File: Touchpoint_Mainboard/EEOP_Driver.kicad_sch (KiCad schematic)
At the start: 3 parts, among them J701 Conn_01x32, J702 Conn_01x32, U701 HV507PG-G

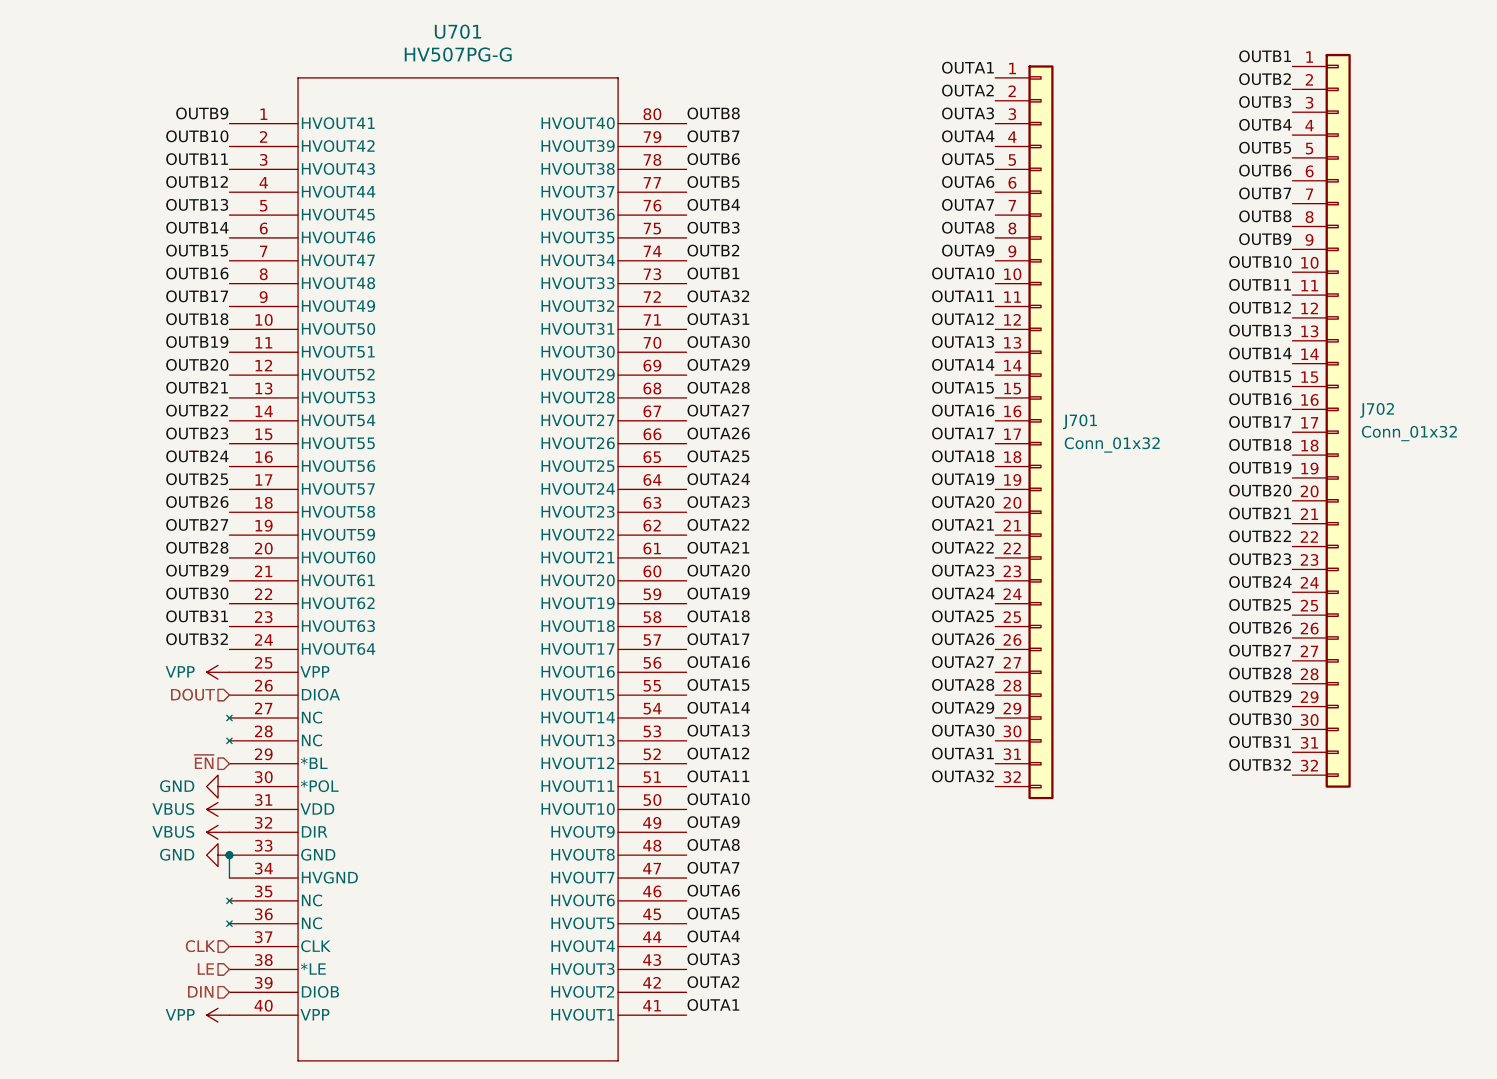
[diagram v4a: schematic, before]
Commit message: Finally finished routing EEOP driver
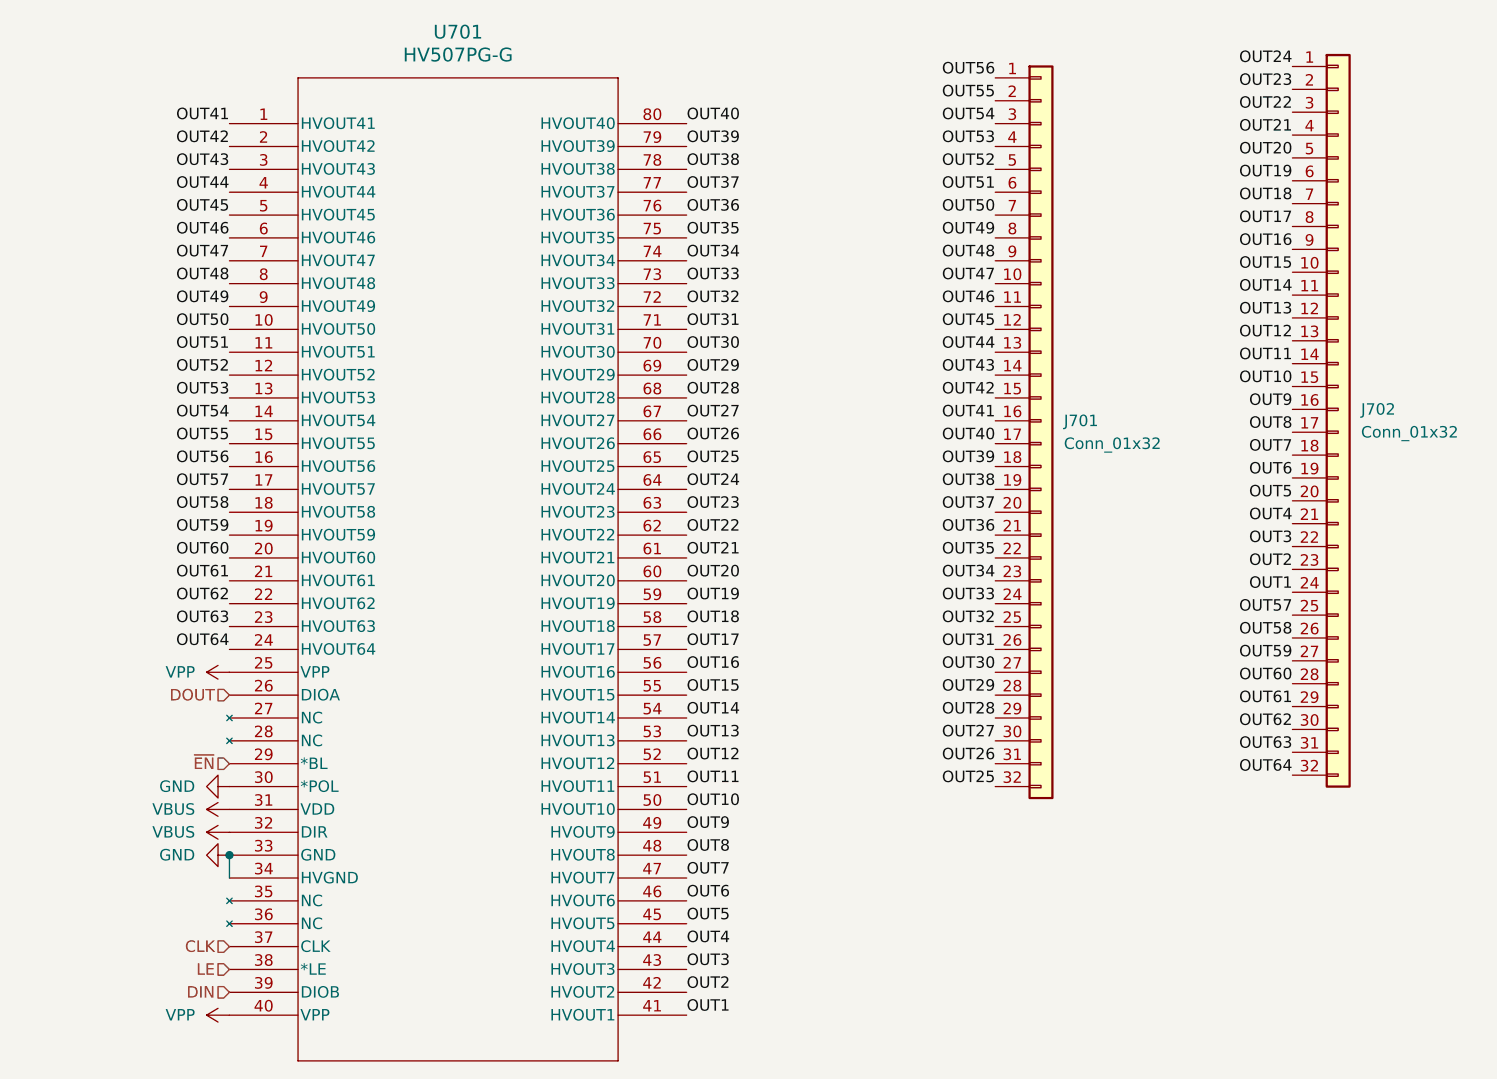
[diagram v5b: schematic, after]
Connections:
- net OUTA1 renamed OUT1
- net OUT1: now also J702.24 (Pin_24); no longer J701.1 (Pin_1)
- net OUTA10 renamed OUT10
- net OUT10: now also J702.15 (Pin_15); no longer J701.10 (Pin_10)
- net OUTA11 renamed OUT11
- net OUT11: now also J702.14 (Pin_14); no longer J701.11 (Pin_11)
- net OUTA12 renamed OUT12
- net OUT12: now also J702.13 (Pin_13); no longer J701.12 (Pin_12)
- net OUTA13 renamed OUT13
- net OUT13: now also J702.12 (Pin_12); no longer J701.13 (Pin_13)
- net OUTA14 renamed OUT14
- net OUT14: now also J702.11 (Pin_11); no longer J701.14 (Pin_14)
- net OUTA15 renamed OUT15
- net OUT15: now also J702.10 (Pin_10); no longer J701.15 (Pin_15)
- net OUTA16 renamed OUT16
- net OUT16: now also J702.9 (Pin_9); no longer J701.16 (Pin_16)
- net OUTA17 renamed OUT17
- net OUT17: now also J702.8 (Pin_8); no longer J701.17 (Pin_17)
- net OUTA18 renamed OUT18
- net OUT18: now also J702.7 (Pin_7); no longer J701.18 (Pin_18)
- net OUTA19 renamed OUT19
- net OUT19: now also J702.6 (Pin_6); no longer J701.19 (Pin_19)
- net OUTA2 renamed OUT2
- net OUT2: now also J702.23 (Pin_23); no longer J701.2 (Pin_2)
- net OUTA20 renamed OUT20
- net OUT20: now also J702.5 (Pin_5); no longer J701.20 (Pin_20)
- net OUTA21 renamed OUT21
- net OUT21: now also J702.4 (Pin_4); no longer J701.21 (Pin_21)
- net OUTA22 renamed OUT22
- net OUT22: now also J702.3 (Pin_3); no longer J701.22 (Pin_22)
- net OUTA23 renamed OUT23
- net OUT23: now also J702.2 (Pin_2); no longer J701.23 (Pin_23)
- net OUTA24 renamed OUT24
- net OUT24: now also J702.1 (Pin_1); no longer J701.24 (Pin_24)
- net OUTA25 renamed OUT25
- net OUT25: now also J701.32 (Pin_32); no longer J701.25 (Pin_25)
- net OUTA26 renamed OUT26
- net OUT26: now also J701.31 (Pin_31); no longer J701.26 (Pin_26)
- net OUTA27 renamed OUT27
- net OUT27: now also J701.30 (Pin_30); no longer J701.27 (Pin_27)
- net OUTA28 renamed OUT28
- net OUT28: now also J701.29 (Pin_29); no longer J701.28 (Pin_28)
- net OUTA29 renamed OUT29
- net OUT29: now also J701.28 (Pin_28); no longer J701.29 (Pin_29)
- net OUTA3 renamed OUT3
- net OUT3: now also J702.22 (Pin_22); no longer J701.3 (Pin_3)
- net OUTA30 renamed OUT30
- net OUT30: now also J701.27 (Pin_27); no longer J701.30 (Pin_30)
- net OUTA31 renamed OUT31
- net OUT31: now also J701.26 (Pin_26); no longer J701.31 (Pin_31)
- net OUTA32 renamed OUT32
- net OUT32: now also J701.25 (Pin_25); no longer J701.32 (Pin_32)
- net OUTA4 renamed OUT4
- net OUT4: now also J702.21 (Pin_21); no longer J701.4 (Pin_4)
- net OUTA5 renamed OUT5
- net OUT5: now also J702.20 (Pin_20); no longer J701.5 (Pin_5)
- net OUTA6 renamed OUT51
- net OUT51: now also U701.11 (HVOUT51); no longer U701.46 (HVOUT6)
- net OUTA7 renamed OUT50
- net OUT50: now also U701.10 (HVOUT50); no longer U701.47 (HVOUT7)
- net OUTA8 renamed OUT49
- net OUT49: now also U701.9 (HVOUT49); no longer U701.48 (HVOUT8)
- net OUTA9 renamed OUT48
- net OUT48: now also U701.8 (HVOUT48); no longer U701.49 (HVOUT9)
- net OUTB1 renamed OUT33
- net OUT33: now also J701.24 (Pin_24); no longer J702.1 (Pin_1)
- net OUTB10 renamed OUT42
- net OUT42: now also J701.15 (Pin_15); no longer J702.10 (Pin_10)
- net OUTB11 renamed OUT43
- net OUT43: now also J701.14 (Pin_14); no longer J702.11 (Pin_11)
- net OUTB12 renamed OUT44
- net OUT44: now also J701.13 (Pin_13); no longer J702.12 (Pin_12)
- net OUTB13 renamed OUT45
- net OUT45: now also J701.12 (Pin_12); no longer J702.13 (Pin_13)
- net OUTB14 renamed OUT46
- net OUT46: now also J701.11 (Pin_11); no longer J702.14 (Pin_14)
- net OUTB15 renamed OUT47
- net OUT47: now also J701.10 (Pin_10); no longer J702.15 (Pin_15)
- net OUTB16 renamed OUT9
- net OUT9: now also U701.49 (HVOUT9); no longer U701.8 (HVOUT48)
- net OUTB17 renamed OUT8
- net OUT8: now also U701.48 (HVOUT8); no longer U701.9 (HVOUT49)
- net OUTB18 renamed OUT7
- net OUT7: now also U701.47 (HVOUT7); no longer U701.10 (HVOUT50)
- net OUTB19 renamed OUT6
- net OUT6: now also U701.46 (HVOUT6); no longer U701.11 (HVOUT51)
- net OUTB2 renamed OUT34
- net OUT34: now also J701.23 (Pin_23); no longer J702.2 (Pin_2)
- net OUTB20 renamed OUT52
- net OUT52: now also J701.5 (Pin_5); no longer J702.20 (Pin_20)
- net OUTB21 renamed OUT53
- net OUT53: now also J701.4 (Pin_4); no longer J702.21 (Pin_21)
- net OUTB22 renamed OUT54
- net OUT54: now also J701.3 (Pin_3); no longer J702.22 (Pin_22)
- net OUTB23 renamed OUT55
- net OUT55: now also J701.2 (Pin_2); no longer J702.23 (Pin_23)
- net OUTB24 renamed OUT56
- net OUT56: now also J701.1 (Pin_1); no longer J702.24 (Pin_24)
- net OUTB25 renamed OUT57
- net OUTB26 renamed OUT58
- net OUTB27 renamed OUT59
- net OUTB28 renamed OUT60
- net OUTB29 renamed OUT61
- net OUTB3 renamed OUT35
- net OUT35: now also J701.22 (Pin_22); no longer J702.3 (Pin_3)
- net OUTB30 renamed OUT62
- net OUTB31 renamed OUT63
- net OUTB32 renamed OUT64
- net OUTB4 renamed OUT36
- net OUT36: now also J701.21 (Pin_21); no longer J702.4 (Pin_4)
- net OUTB5 renamed OUT37
- net OUT37: now also J701.20 (Pin_20); no longer J702.5 (Pin_5)
- net OUTB6 renamed OUT38
- net OUT38: now also J701.19 (Pin_19); no longer J702.6 (Pin_6)
- net OUTB7 renamed OUT39
- net OUT39: now also J701.18 (Pin_18); no longer J702.7 (Pin_7)
- net OUTB8 renamed OUT40
- net OUT40: now also J701.17 (Pin_17); no longer J702.8 (Pin_8)
- net OUTB9 renamed OUT41
- net OUT41: now also J701.16 (Pin_16); no longer J702.9 (Pin_9)

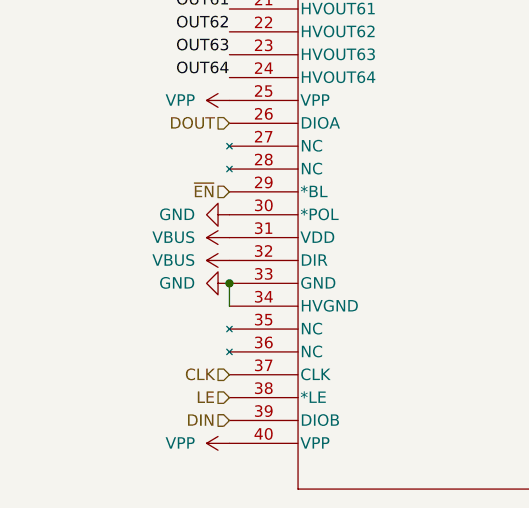
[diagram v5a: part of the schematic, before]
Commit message: Almost finished routing mainboard
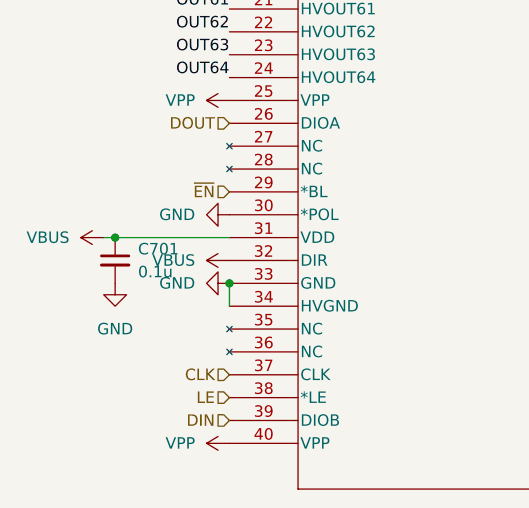
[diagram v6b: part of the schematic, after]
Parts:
- added C701: 0.1u, Capacitor_SMD:C_0402_1005Metric, symbol Device:C_Small
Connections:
- net GND: now also C701.2
- net VBUS: now also C701.1
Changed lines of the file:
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@@
 		(color 0 0 0 0)
+	)
+	(junction
+		(at 13.97 100.33)
+		(diameter 0)
+		(color 0 0 0 0)
+	)
+	(wire
+		(pts
+			(xy 13.97 100.33) (xy 26.67 100.33)
+		)
+		(stroke
+			(width 0)
+			(type default)
+		)
+	)
+	(wire
+		(pts
+			(xy 12.7 100.33) (xy 13.97 100.33)
+		)
+		(stroke
+			(width 0)
+			(type default)
+		)
 	)
 	(wire
@@
 	)
 	(symbol
+		(lib_id "Device:C_Small")
+		(at 13.97 102.87 0)
+		(unit 1)
+		(exclude_from_sim no)
+		(in_bom yes)
+		(on_board yes)
+		(dnp no)
+		(fields_autoplaced yes)
+		(property "Reference" "C701"
+			(at 16.51 101.6062 0)
+			(effects
+				(font
+					(size 1.27 1.27)
+				)
+				(justify left)
+			)
+		)
+		(property "Value" "0.1u"
+			(at 16.51 104.1462 0)
+			(effects
+				(font
+					(size 1.27 1.27)
+				)
+				(justify left)
+			)
+		)
+		(property "Footprint" "Capacitor_SMD:C_0402_1005Metric"
+			(at 13.97 102.87 0)
+			(effects
+				(font
+					(size 1.27 1.27)
+				)
+				(hide yes)
+			)
+		)
+		(property "Datasheet" "~"
+			(at 13.97 102.87 0)
+			(effects
+				(font
+					(size 1.27 1.27)
+				)
+				(hide yes)
+			)
+		)
+		(property "Description" "Unpolarized capacitor, small symbol"
+			(at 13.97 102.87 0)
+			(effects
+				(font
+					(size 1.27 1.27)
+				)
+				(hide yes)
+			)
+		)
+		(pin "2"
+		)
+		(pin "1"
+		)
+		(instances
+			(project "Touchpoint_Mainboard"
+				(path "/f37b5f88-420a-4646-85df-8f9851d23e3c/d77d4631-394e-42d9-bdcc-1bd3eb66f861"
+					(reference "C701")
+					(unit 1)
+				)
+			)
+		)
+	)
+	(symbol
+		(lib_id "power:GND")
+		(at 13.97 105.41 0)
+		(unit 1)
+		(exclude_from_sim no)
+		(in_bom yes)
+		(on_board yes)
+		(dnp no)
+		(fields_autoplaced yes)
+		(property "Reference" "#PWR0707"
+			(at 13.97 111.76 0)
+			(effects
+				(font
+					(size 1.27 1.27)
+				)
+				(hide yes)
+			)
+		)
+		(property "Value" "GND"
+			(at 13.97 110.49 0)
+			(effects
+				(font
+					(size 1.27 1.27)
+				)
+			)
+		)
+		(property "Footprint" ""
+			(at 13.97 105.41 0)
+			(effects
+				(font
+					(size 1.27 1.27)
+				)
+				(hide yes)
+			)
+		)
+		(property "Datasheet" ""
+			(at 13.97 105.41 0)
+			(effects
+				(font
+					(size 1.27 1.27)
+				)
+				(hide yes)
+			)
+		)
+		(property "Description" "Power symbol creates a global label with name \"GND\" , ground"
+			(at 13.97 105.41 0)
+			(effects
+				(font
+					(size 1.27 1.27)
+				)
+				(hide yes)
+			)
+		)
+		(pin "1"
+		)
+		(instances
+			(project ""
+				(path "/f37b5f88-420a-4646-85df-8f9851d23e3c/d77d4631-394e-42d9-bdcc-1bd3eb66f861"
+					(reference "#PWR0707")
+					(unit 1)
+				)
+			)
+		)
+	)
+	(symbol
 		(lib_id "power:VPP")
 		(at 26.67 123.19 90)
@@
 	(symbol
 		(lib_id "power:+5V")
-		(at 26.67 100.33 90)
+		(at 12.7 100.33 90)
 		(unit 1)
 		(exclude_from_sim no)
@@
 		(fields_autoplaced yes)
 		(property "Reference" "#PWR0703"
-			(at 30.48 100.33 0)
+			(at 16.51 100.33 0)
 			(effects
 				(font
@@
 		)
 		(property "Value" "VBUS"
-			(at 22.86 100.3299 90)
+			(at 8.89 100.3299 90)
 			(effects
 				(font
@@
 		)
 		(property "Footprint" ""
-			(at 26.67 100.33 0)
+			(at 12.7 100.33 0)
 			(effects
 				(font
@@
 		)
 		(property "Datasheet" ""
-			(at 26.67 100.33 0)
+			(at 12.7 100.33 0)
 			(effects
 				(font
@@
 		)
 		(property "Description" "Power symbol creates a global label with name \"+5V\""
-			(at 26.67 100.33 0)
-			(effects
-				(font
+			(at 12.7 100.33 0)
+			(effects
+				(font
